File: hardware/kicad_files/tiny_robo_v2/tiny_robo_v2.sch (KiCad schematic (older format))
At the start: 33 parts, among them P1 CONN_8, P2 BATT, P3 CONN_01X02, P4 CONNECTOR, P5 CONNECTOR, P6 CONN_01X02, SW1 SPDT, U1 MCP73831, U2 MIC5265, U3 ESP8266-ESP-03, U4 DRV8830, U5 DRV8830

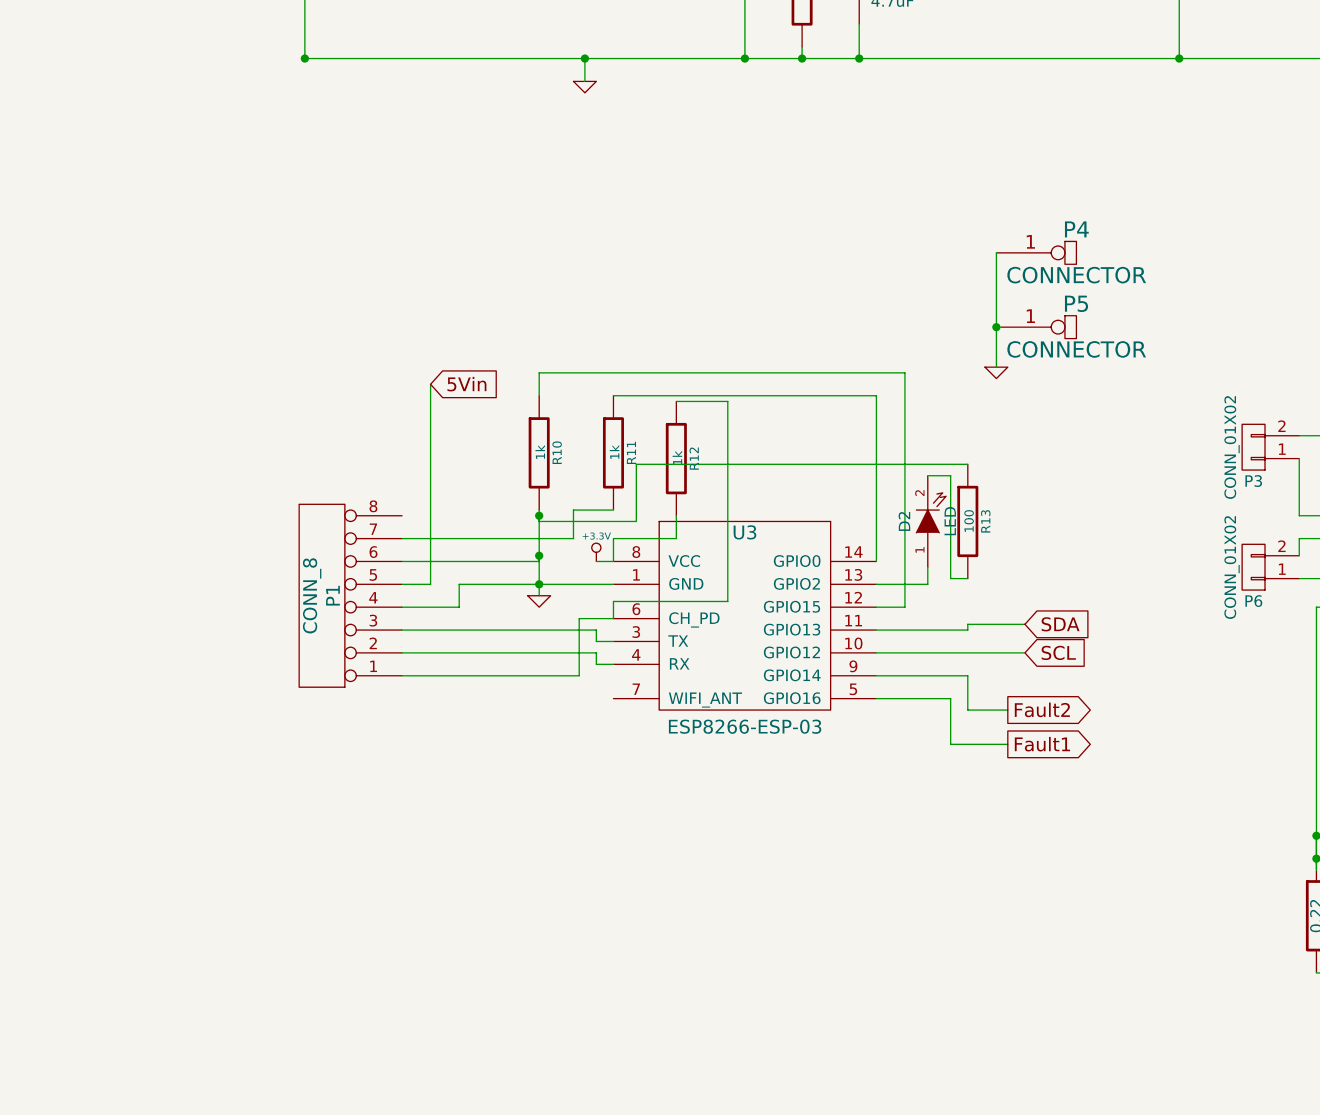
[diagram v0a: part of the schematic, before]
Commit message: Added pull-ups and conections for 'ck' reset method. I've modifed my FTDI dongle to upload it, will test on breadboard soon.
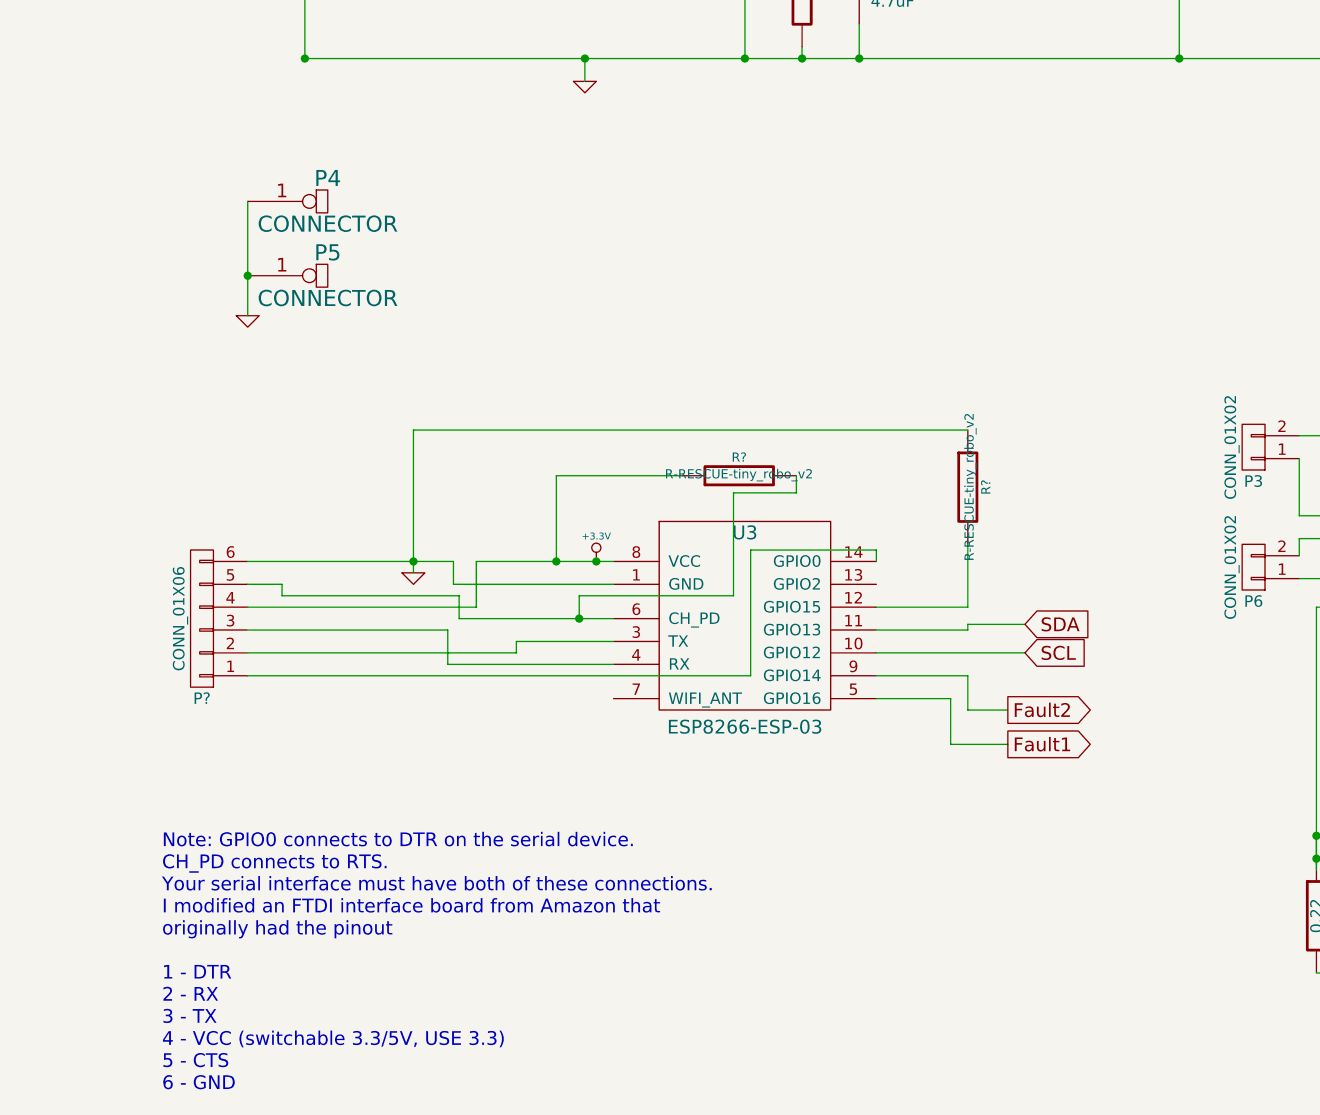
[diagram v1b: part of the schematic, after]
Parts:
- removed D2: LED, LEDs:LED-0805, symbol LED-RESCUE-tiny_robo_v2
- removed P1: CONN_8, Pin_Headers:Pin_Header_Straight_1x08, symbol CONN_8
- removed R10, R11, R12: 1k, Resistors_SMD:R_1206_HandSoldering, symbol R-RESCUE-tiny_robo_v2
- removed R13: 100, Resistors_SMD:R_1206_HandSoldering, symbol R-RESCUE-tiny_robo_v2
- added P?: CONN_01X06, symbol CONN_01X06
- added R? (x2): R-RESCUE-tiny_robo_v2, symbol R-RESCUE-tiny_robo_v2
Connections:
- net +3.3V: now also P?.4 (P4), R?.1
- net GND: now also P?.6 (P6), R?.1
- net at U3.12 (GPIO15): now also R?.2
- net at U3.14 (GPIO0): now also P?.1 (P1)
- net at U3.3 (TX): now also P?.2 (P2)
- net at U3.4 (RX): now also P?.3 (P3)
- net at U3.6 (CH_PD): now also P?.5 (P5), R?.2
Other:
- note added: "Note: GPIO0 connects to DTR on the serial device. \nCH_PD connects to RTS. \nYour serial interface must have both of these connections. \nI modified an FTDI interface board from Amazon that \noriginally had the pinout \n\n1 - DTR\n2 - RX\n3 - TX \n4 - VCC (switchable 3.3/5V, USE 3.3)\n5 - CTS\n6 - GND"
- moved on the sheet: P4, P5
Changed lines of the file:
@@
 EESchema Schematic File Version 2
-LIBS:tiny_robo_v2-rescue
 LIBS:power
 LIBS:device
@@
 Text GLabel 1525 1850 0    60   Input ~ 0
 5Vin
-Text GLabel 3775 4025 2    60   Input ~ 0
-5Vin
 Text GLabel 6300 5450 2    60   Output ~ 0
 Fault2
@@
 $EndComp
 $Comp
-L GND-RESCUE-tiny_robo_v2 #PWR04
-U 1 1 5575FDC6
-P 4250 4950
-F 0 "#PWR04" H 4250 4950 30  0001 C CNN
-F 1 "GND" H 4250 4880 30  0001 C CNN
-F 2 "" H 4250 4950 60  0001 C CNN
-F 3 "" H 4250 4950 60  0001 C CNN
-	1    4250 4950
-	1    0    0    -1
-$EndComp
-$Comp
 L +3.3V-RESCUE-tiny_robo_v2 #PWR05
 U 1 1 5575F5D2
@@
 F 3 "" H 4500 4800 60  0001 C CNN
 	1    4500 4800
-	1    0    0    -1
-$EndComp
-$Comp
-L ESP8266-ESP-03 U3
-U 1 1 5575F418
-P 5150 5400
-F 0 "U3" H 5150 6125 60  0000 C CNN
-F 1 "ESP8266-ESP-03" H 5150 5275 60  0000 C CNN
-F 2 "esp-8266:ESP8266-ESP-03" H 5150 5400 60  0001 C CNN
-F 3 "" H 5150 5400 60  0001 C CNN
-	1    5150 5400
 	1    0    0    -1
 $EndComp
@@
 Wire Wire Line
 	8375 4500 8375 4900
-Wire Wire Line
-	3650 4900 3775 4900
 Connection ~ 3225 2600
 Wire Wire Line
@@
 	9175 4900 9450 4900
 Wire Wire Line
-	4575 4800 4500 4800
+	3975 4800 4575 4800
 Connection ~ 5650 1850
 Wire Wire Line
@@
 Connection ~ 7050 2600
 Wire Wire Line
-	4250 4575 4250 4950
-Wire Wire Line
 	9650 5000 9175 5000
 Wire Wire Line
@@
 	6475 1425 6475 1300
 Wire Wire Line
-	4575 4900 3900 4900
-Wire Wire Line
-	3900 4900 3900 5000
-Wire Wire Line
-	3900 5000 3650 5000
-Connection ~ 4250 4900
-Wire Wire Line
-	3775 4900 3775 4025
-Wire Wire Line
 	1525 1850 2025 1850
 Wire Wire Line
@@
 Connection ~ 7650 6000
 Connection ~ 7650 6100
-Wire Wire Line
-	3650 5300 4425 5300
-Wire Wire Line
-	4425 5300 4425 5050
-Wire Wire Line
-	4425 5050 4575 5050
-Wire Wire Line
-	3650 5200 4500 5200
-Wire Wire Line
-	4500 5200 4500 5250
-Wire Wire Line
-	4500 5250 4575 5250
-Wire Wire Line
-	4575 5150 4500 5150
-Wire Wire Line
-	4500 5150 4500 5100
-Wire Wire Line
-	4500 5100 3650 5100
 $Comp
 L SPDT-RESCUE-tiny_robo_v2 SW1
@@
 L CONNECTOR P4
 U 1 1 559D6607
-P 6250 3450
-F 0 "P4" H 6600 3550 70  0000 C CNN
-F 1 "CONNECTOR" H 6600 3350 70  0000 C CNN
-F 2 "Wire_Pads:SolderWirePad_single_0-8mmDrill" H 6250 3450 60  0001 C CNN
-F 3 "" H 6250 3450 60  0000 C CNN
-	1    6250 3450
+P 2975 3225
+F 0 "P4" H 3325 3325 70  0000 C CNN
+F 1 "CONNECTOR" H 3325 3125 70  0000 C CNN
+F 2 "Wire_Pads:SolderWirePad_single_0-8mmDrill" H 2975 3225 60  0001 C CNN
+F 3 "" H 2975 3225 60  0000 C CNN
+	1    2975 3225
 	1    0    0    -1
 $EndComp
@@
 L CONNECTOR P5
 U 1 1 559D66C8
-P 6250 3775
-F 0 "P5" H 6600 3875 70  0000 C CNN
-F 1 "CONNECTOR" H 6600 3675 70  0000 C CNN
-F 2 "Wire_Pads:SolderWirePad_single_0-8mmDrill" H 6250 3775 60  0001 C CNN
-F 3 "" H 6250 3775 60  0000 C CNN
-	1    6250 3775
-	1    0    0    -1
-$EndComp
-Wire Wire Line
-	6250 3450 6250 3950
+P 2975 3550
+F 0 "P5" H 3325 3650 70  0000 C CNN
+F 1 "CONNECTOR" H 3325 3450 70  0000 C CNN
+F 2 "Wire_Pads:SolderWirePad_single_0-8mmDrill" H 2975 3550 60  0001 C CNN
+F 3 "" H 2975 3550 60  0000 C CNN
+	1    2975 3550
+	1    0    0    -1
+$EndComp
+Wire Wire Line
+	2975 3225 2975 3725
 $Comp
 L GND-RESCUE-tiny_robo_v2 #PWR09
 U 1 1 559D6D0E
-P 6250 3950
-F 0 "#PWR09" H 6250 3950 30  0001 C CNN
-F 1 "GND" H 6250 3880 30  0001 C CNN
-F 2 "" H 6250 3950 60  0000 C CNN
-F 3 "" H 6250 3950 60  0000 C CNN
-	1    6250 3950
-	1    0    0    -1
-$EndComp
-Connection ~ 6250 3775
+P 2975 3725
+F 0 "#PWR09" H 2975 3725 30  0001 C CNN
+F 1 "GND" H 2975 3655 30  0001 C CNN
+F 2 "" H 2975 3725 60  0000 C CNN
+F 3 "" H 2975 3725 60  0000 C CNN
+	1    2975 3725
+	1    0    0    -1
+$EndComp
+Connection ~ 2975 3550
 $Comp
 L CONN_01X02 P3
@@
 	6050 5600 6300 5600
 $Comp
-L R-RESCUE-tiny_robo_v2 R11
-U 1 1 566F3103
-P 4575 4325
-F 0 "R11" V 4655 4325 40  0000 C CNN
-F 1 "1k" V 4582 4326 40  0000 C CNN
-F 2 "Resistors_SMD:R_1206_HandSoldering" V 4505 4325 30  0001 C CNN
-F 3 "" H 4575 4325 30  0000 C CNN
-	1    4575 4325
-	1    0    0    -1
-$EndComp
-$Comp
-L R-RESCUE-tiny_robo_v2 R10
-U 1 1 566F32C9
-P 4250 4325
-F 0 "R10" V 4330 4325 40  0000 C CNN
-F 1 "1k" V 4257 4326 40  0000 C CNN
-F 2 "Resistors_SMD:R_1206_HandSoldering" V 4180 4325 30  0001 C CNN
-F 3 "" H 4250 4325 30  0000 C CNN
-	1    4250 4325
-	1    0    0    -1
-$EndComp
-Wire Wire Line
-	4575 4075 5725 4075
-Wire Wire Line
-	5725 4075 5725 4800
-Wire Wire Line
-	5725 5000 5850 5000
-Wire Wire Line
-	5850 5000 5850 3975
-Wire Wire Line
-	5850 3975 4250 3975
-Wire Wire Line
-	4250 3975 4250 4075
-$Comp
-L R-RESCUE-tiny_robo_v2 R12
-U 1 1 566F3E82
-P 4850 4350
-F 0 "R12" V 4930 4350 40  0000 C CNN
-F 1 "1k" V 4857 4351 40  0000 C CNN
-F 2 "Resistors_SMD:R_1206_HandSoldering" V 4780 4350 30  0001 C CNN
-F 3 "" H 4850 4350 30  0000 C CNN
-	1    4850 4350
-	1    0    0    -1
-$EndComp
-Wire Wire Line
-	4575 5050 4575 4975
-Wire Wire Line
-	4575 4975 5075 4975
-Wire Wire Line
-	5075 4975 5075 4100
-Wire Wire Line
-	5075 4100 4850 4100
-Wire Wire Line
-	4575 4800 4575 4700
-Wire Wire Line
-	4575 4700 4850 4700
-Wire Wire Line
-	4850 4700 4850 4600
-$Comp
-L CONN_8 P1
-U 1 1 566F41F0
-P 3300 4950
-F 0 "P1" V 3250 4950 60  0000 C CNN
-F 1 "CONN_8" V 3350 4950 60  0000 C CNN
-F 2 "Pin_Headers:Pin_Header_Straight_1x08" H 3300 4950 60  0001 C CNN
-F 3 "" H 3300 4950 60  0000 C CNN
-	1    3300 4950
+L ESP8266-ESP-03 U3
+U 1 1 5575F418
+P 5150 5400
+F 0 "U3" H 5150 6125 60  0000 C CNN
+F 1 "ESP8266-ESP-03" H 5150 5275 60  0000 C CNN
+F 2 "esp-8266:ESP8266-ESP-03" H 5150 5400 60  0001 C CNN
+F 3 "" H 5150 5400 60  0001 C CNN
+	1    5150 5400
+	1    0    0    -1
+$EndComp
+$Comp
+L CONN_01X06 P?
+U 1 1 570E7DDF
+P 2775 5050
+F 0 "P?" H 2775 5400 50  0000 C CNN
+F 1 "CONN_01X06" V 2875 5050 50  0000 C CNN
+F 2 "" H 2775 5050 50  0000 C CNN
+F 3 "" H 2775 5050 50  0000 C CNN
+	1    2775 5050
 	-1   0    0    1
 $EndComp
 Wire Wire Line
-	3650 4800 4250 4800
-Wire Wire Line
-	4250 4800 4250 4775
-Connection ~ 4250 4775
-Wire Wire Line
-	3650 4700 4400 4700
-Wire Wire Line
-	4400 4700 4400 4575
-Wire Wire Line
-	4400 4575 4575 4575
-$Comp
-L R-RESCUE-tiny_robo_v2 R13
-U 1 1 566F47F1
-P 6125 4625
-F 0 "R13" V 6205 4625 40  0000 C CNN
-F 1 "100" V 6132 4626 40  0000 C CNN
-F 2 "Resistors_SMD:R_1206_HandSoldering" V 6055 4625 30  0001 C CNN
-F 3 "" H 6125 4625 30  0000 C CNN
-	1    6125 4625
-	1    0    0    -1
-$EndComp
-$Comp
-L LED-RESCUE-tiny_robo_v2 D2
-U 1 1 566F4942
-P 5950 4625
-F 0 "D2" H 5950 4725 50  0000 C CNN
-F 1 "LED" H 5950 4525 50  0000 C CNN
-F 2 "LEDs:LED-0805" H 5950 4625 60  0001 C CNN
-F 3 "" H 5950 4625 60  0000 C CNN
-	1    5950 4625
+	2975 5000 3975 5000
+Wire Wire Line
+	3975 5000 3975 4800
+Connection ~ 4500 4800
+Wire Wire Line
+	2975 4800 3875 4800
+Wire Wire Line
+	3875 4800 3875 4900
+Wire Wire Line
+	3875 4900 4575 4900
+Wire Wire Line
+	2975 5200 4150 5200
+Wire Wire Line
+	4150 5200 4150 5150
+Wire Wire Line
+	4150 5150 4575 5150
+Wire Wire Line
+	3850 5250 4575 5250
+Wire Wire Line
+	3850 5250 3850 5100
+Wire Wire Line
+	3850 5100 2975 5100
+Text Notes 2600 7125 0    60   ~ 0
+Note: GPIO0 connects to DTR on the serial device. \nCH_PD connects to RTS. \nYour serial interface must have both of these connections. \nI modified an FTDI interface board from Amazon that \noriginally had the pinout \n\n1 - DTR\n2 - RX\n3 - TX \n4 - VCC (switchable 3.3/5V, USE 3.3)\n5 - CTS\n6 - GND
+Wire Wire Line
+	2975 5300 5175 5300
+Wire Wire Line
+	5175 5300 5175 4750
+Wire Wire Line
+	4575 5050 3900 5050
+Wire Wire Line
+	3900 5050 3900 4950
+Wire Wire Line
+	3900 4950 3125 4950
+Wire Wire Line
+	3125 4950 3125 4900
+Wire Wire Line
+	3125 4900 2975 4900
+$Comp
+L GND-RESCUE-tiny_robo_v2 #PWR?
+U 1 1 570E86D9
+P 3700 4850
+F 0 "#PWR?" H 3700 4850 30  0001 C CNN
+F 1 "GND-RESCUE-tiny_robo_v2" H 3700 4780 30  0001 C CNN
+F 2 "" H 3700 4850 60  0000 C CNN
+F 3 "" H 3700 4850 60  0000 C CNN
+	1    3700 4850
+	1    0    0    -1
+$EndComp
+Wire Wire Line
+	3700 4225 3700 4850
+Connection ~ 3700 4800
+$Comp
+L R-RESCUE-tiny_robo_v2 R?
+U 1 1 570E8A3E
+P 5125 4425
+F 0 "R?" V 5205 4425 40  0000 C CNN
+F 1 "R-RESCUE-tiny_robo_v2" V 5132 4426 40  0000 C CNN
+F 2 "" V 5055 4425 30  0000 C CNN
+F 3 "" H 5125 4425 30  0000 C CNN
+	1    5125 4425
 	0    -1   -1   0
 $EndComp
-Wire Wire Line
-	5725 4900 5950 4900
-Wire Wire Line
-	5950 4900 5950 4825
-Wire Wire Line
-	5950 4425 6050 4425
-Wire Wire Line
-	6050 4425 6050 4875
-Wire Wire Line
-	6050 4875 6125 4875
-Wire Wire Line
-	6125 4375 4675 4375
-Wire Wire Line
-	4675 4375 4675 4625
-Wire Wire Line
-	4675 4625 4250 4625
-Wire Wire Line
-	4250 4625 4250 4600
-Connection ~ 4250 4600
+$Comp
+L R-RESCUE-tiny_robo_v2 R?
+U 1 1 570E8B63
+P 6125 4475
+F 0 "R?" V 6205 4475 40  0000 C CNN
+F 1 "R-RESCUE-tiny_robo_v2" V 6132 4476 40  0000 C CNN
+F 2 "" V 6055 4475 30  0000 C CNN
+F 3 "" H 6125 4475 30  0000 C CNN
+	1    6125 4475
+	1    0    0    -1
+$EndComp
+Wire Wire Line
+	5725 5000 6125 5000
+Wire Wire Line
+	6125 5000 6125 4725
+Wire Wire Line
+	5175 4750 5725 4750
+Wire Wire Line
+	5725 4750 5725 4800
+Wire Wire Line
+	4425 5050 4425 4950
+Wire Wire Line
+	4425 4950 5100 4950
+Wire Wire Line
+	5100 4950 5100 4500
+Wire Wire Line
+	5100 4500 5375 4500
+Wire Wire Line
+	5375 4500 5375 4425
+Connection ~ 4425 5050
+Wire Wire Line
+	4875 4425 4325 4425
+Wire Wire Line
+	4325 4425 4325 4800
+Connection ~ 4325 4800
+Wire Wire Line
+	3700 4225 6125 4225
 $EndSCHEMATC

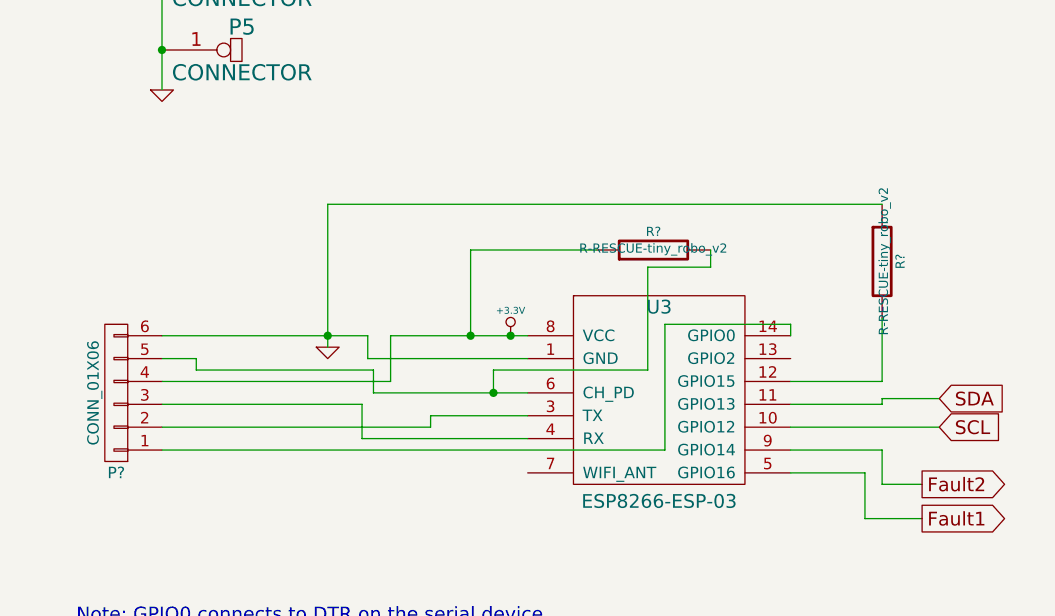
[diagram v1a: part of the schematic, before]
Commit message: Removed VCC connection on upload header, just turn the robot on to upload. Powering from USB is unreliable.
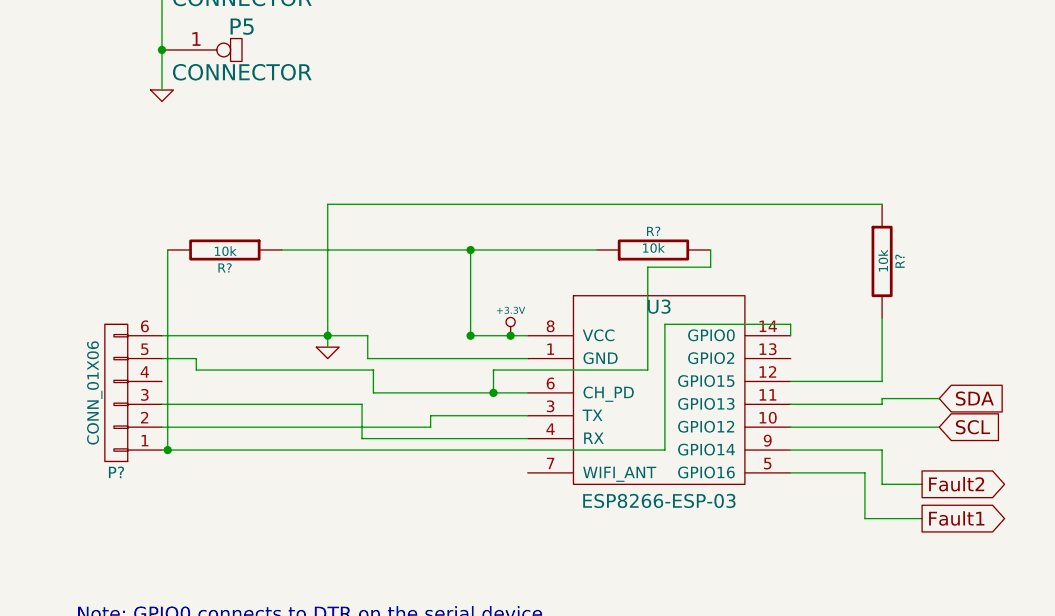
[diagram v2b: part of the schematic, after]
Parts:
- added R?: 10k, symbol R-RESCUE-tiny_robo_v2
- R? (x2): value R-RESCUE-tiny_robo_v2 -> 10k
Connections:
- net +3.3V: now also R?.1; no longer P?.4 (P4)
- net at P?.1 (P1), U3.14 (GPIO0): now also R?.2
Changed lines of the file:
@@
 Wire Wire Line
 	9175 4900 9450 4900
-Wire Wire Line
-	3975 4800 4575 4800
 Connection ~ 5650 1850
 Wire Wire Line
@@
 	-1   0    0    1
 $EndComp
-Wire Wire Line
-	2975 5000 3975 5000
-Wire Wire Line
-	3975 5000 3975 4800
 Connection ~ 4500 4800
 Wire Wire Line
@@
 P 5125 4425
 F 0 "R?" V 5205 4425 40  0000 C CNN
-F 1 "R-RESCUE-tiny_robo_v2" V 5132 4426 40  0000 C CNN
+F 1 "10k" V 5132 4426 40  0000 C CNN
 F 2 "" V 5055 4425 30  0000 C CNN
 F 3 "" H 5125 4425 30  0000 C CNN
@@
 P 6125 4475
 F 0 "R?" V 6205 4475 40  0000 C CNN
-F 1 "R-RESCUE-tiny_robo_v2" V 6132 4476 40  0000 C CNN
+F 1 "10k" V 6132 4476 40  0000 C CNN
 F 2 "" V 6055 4475 30  0000 C CNN
 F 3 "" H 6125 4475 30  0000 C CNN
@@
 Connection ~ 4425 5050
 Wire Wire Line
-	4875 4425 4325 4425
+	3500 4425 4875 4425
 Wire Wire Line
 	4325 4425 4325 4800
@@
 Wire Wire Line
 	3700 4225 6125 4225
+$Comp
+L R-RESCUE-tiny_robo_v2 R?
+U 1 1 57156590
+P 3250 4425
+F 0 "R?" V 3330 4425 40  0000 C CNN
+F 1 "10k" V 3257 4426 40  0000 C CNN
+F 2 "" V 3180 4425 30  0000 C CNN
+F 3 "" H 3250 4425 30  0000 C CNN
+	1    3250 4425
+	0    1    1    0
+$EndComp
+Connection ~ 4325 4425
+Wire Wire Line
+	3000 4425 3000 5300
+Connection ~ 3000 5300
+Wire Wire Line
+	4325 4800 4575 4800
 $EndSCHEMATC
